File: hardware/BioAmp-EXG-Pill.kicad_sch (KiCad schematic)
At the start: 27 parts, among them J1 BioAmp Output, J2 BioAmp Input, U1 Amp, U2 LOGO_UDLABS

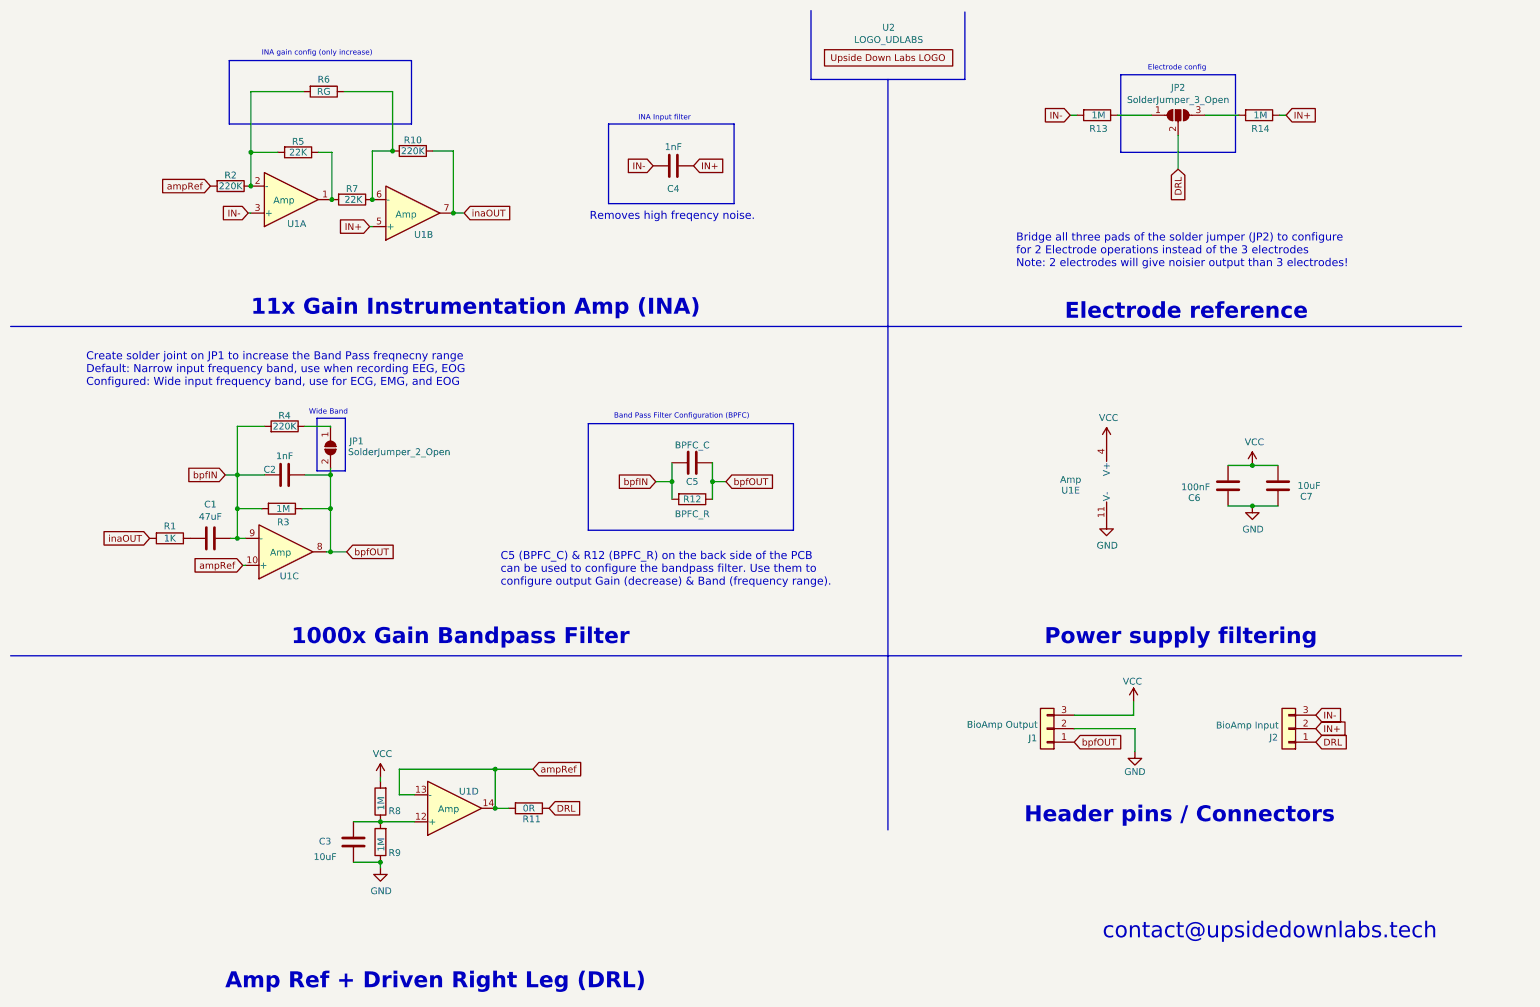
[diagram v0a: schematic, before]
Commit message: shrink the pcb's dimensions
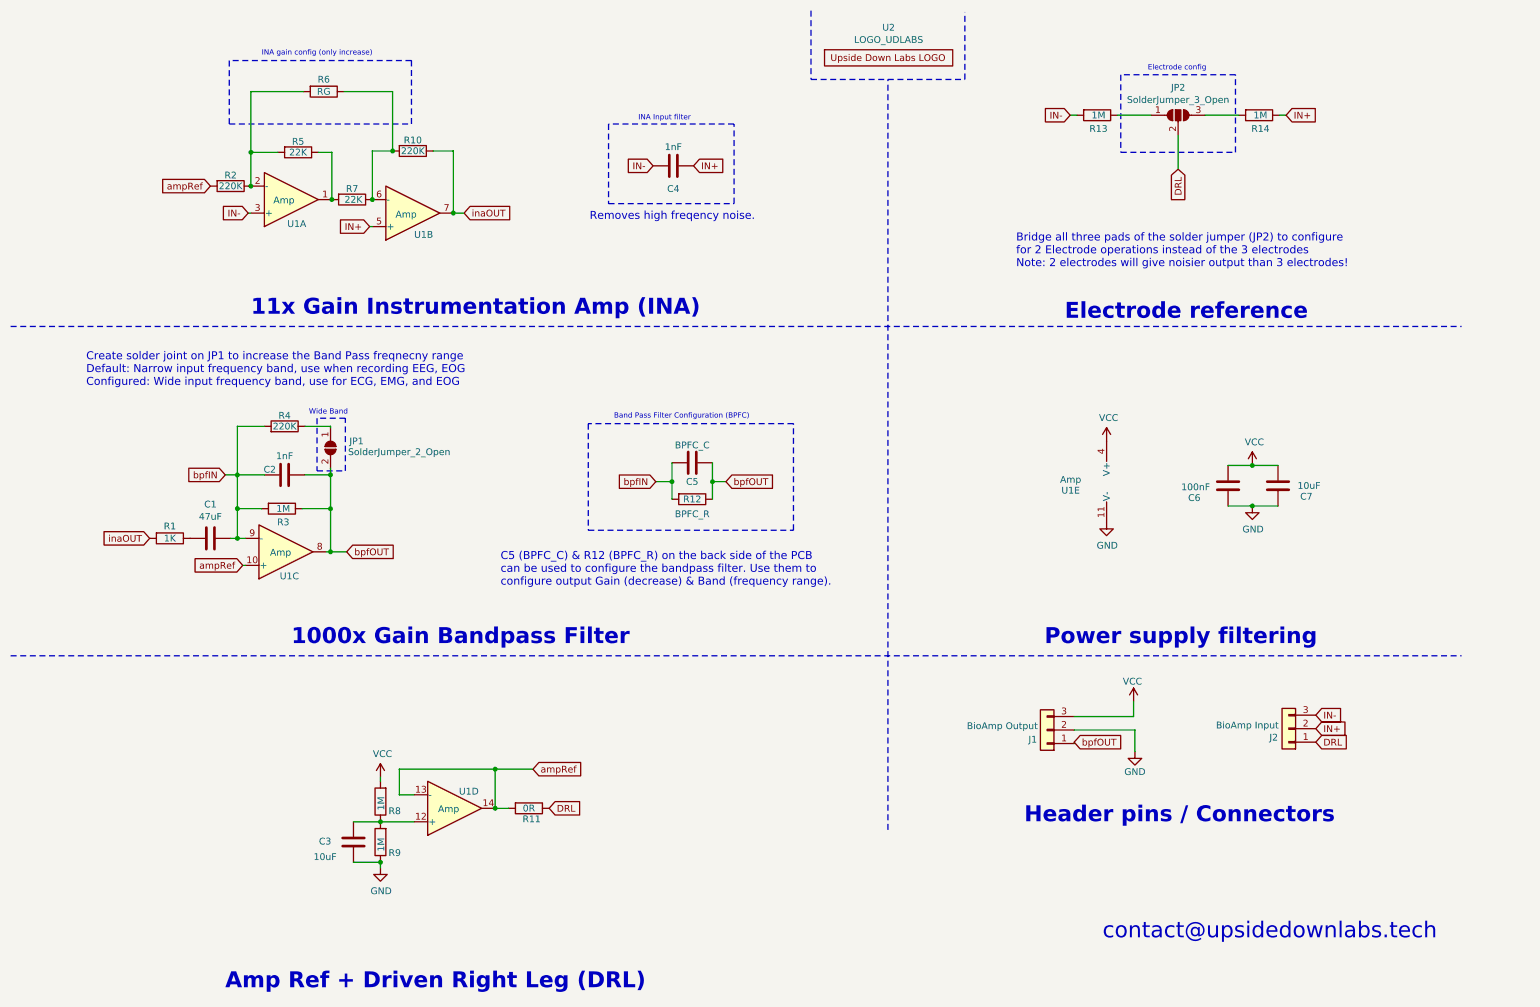
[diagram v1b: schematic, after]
